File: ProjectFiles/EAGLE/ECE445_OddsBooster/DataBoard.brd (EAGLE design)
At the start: 100 x 80 mm, 51 parts, among them U2 74LV164D-SHIFT_REGISTER, U3 74LV164D-SHIFT_REGISTER, U4 74LV164D-SHIFT_REGISTER, X1 FH12-40S-0.5SH

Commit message: layout minor changes
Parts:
- moved R13 90.6 mm to (29.0, 35.1)
- moved MIC2169 77.0 mm to (20.2, 26.4)
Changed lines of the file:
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@@
 <attribute name="VALUE" x="1.397" y="-7.5565" size="1.27" layer="27"/>
 </element>
-<element name="MIC2169" library="pinhead" library_urn="urn:adsk.eagle:library:325" package="2X05" package3d_urn="urn:adsk.eagle:package:22470/2" value="" x="6.858" y="-49.403" smashed="yes">
-<attribute name="NAME" x="0.508" y="-46.228" size="1.27" layer="25" ratio="10"/>
-<attribute name="POPULARITY" value="35" x="6.858" y="-30.861" size="1.778" layer="27" display="off"/>
-<attribute name="VALUE" x="0.508" y="-53.848" size="1.27" layer="27"/>
+<element name="MIC2169" library="pinhead" library_urn="urn:adsk.eagle:library:325" package="2X05" package3d_urn="urn:adsk.eagle:package:22470/2" value="" x="20.193" y="26.416" smashed="yes">
+<attribute name="NAME" x="13.843" y="29.591" size="1.27" layer="25" ratio="10"/>
+<attribute name="POPULARITY" value="35" x="20.193" y="44.958" size="1.778" layer="27" display="off"/>
+<attribute name="VALUE" x="13.843" y="21.971" size="1.27" layer="27"/>
 </element>
 <element name="R9" library="rcl" library_urn="urn:adsk.eagle:library:334" package="R0805" package3d_urn="urn:adsk.eagle:package:23553/2" value="4k" x="11.43" y="-67.564" smashed="yes">
@@
 <attribute name="VALUE" x="4.318" y="-57.658" size="1.27" layer="27" ratio="10"/>
 </element>
-<element name="R13" library="rcl" library_urn="urn:adsk.eagle:library:334" package="R0805" package3d_urn="urn:adsk.eagle:package:23553/2" value="1.5k" x="20.574" y="-55.118" smashed="yes">
-<attribute name="NAME" x="19.939" y="-53.848" size="1.27" layer="25"/>
-<attribute name="POPULARITY" value="85" x="2.032" y="-112.522" size="1.778" layer="27" display="off"/>
-<attribute name="SPICEPREFIX" value="R" x="2.032" y="-112.522" size="1.778" layer="27" display="off"/>
-<attribute name="VALUE" x="19.939" y="-57.658" size="1.27" layer="27"/>
+<element name="R13" library="rcl" library_urn="urn:adsk.eagle:library:334" package="R0805" package3d_urn="urn:adsk.eagle:package:23553/2" value="1.5k" x="28.956" y="35.052" smashed="yes">
+<attribute name="NAME" x="28.321" y="36.322" size="1.27" layer="25"/>
+<attribute name="POPULARITY" value="85" x="10.414" y="-22.352" size="1.778" layer="27" display="off"/>
+<attribute name="SPICEPREFIX" value="R" x="10.414" y="-22.352" size="1.778" layer="27" display="off"/>
+<attribute name="VALUE" x="28.321" y="32.512" size="1.27" layer="27"/>
 </element>
 <element name="R14" library="pot" library_urn="urn:adsk.eagle:library:331" package="3223G" package3d_urn="urn:adsk.eagle:package:22722/1" value="1k" x="17.78" y="-29.972" smashed="yes">
@@
 <wire x1="6.985" y1="-24.13" x2="7.173" y2="-17.399" width="0" layer="19" extent="1-1"/>
 <wire x1="15.58" y1="-28.572" x2="6.985" y2="-24.13" width="0" layer="19" extent="1-1"/>
-<wire x1="11.938" y1="-48.133" x2="15.58" y2="-28.572" width="0" layer="19" extent="1-1"/>
-<wire x1="8.189" y1="-61.341" x2="11.938" y2="-48.133" width="0" layer="19" extent="1-1"/>
+<wire x1="25.273" y1="27.686" x2="15.58" y2="-28.572" width="0" layer="19" extent="1-1"/>
+<wire x1="8.189" y1="-61.341" x2="25.273" y2="27.686" width="0" layer="19" extent="1-1"/>
 <wire x1="2.982" y1="-61.341" x2="8.189" y2="-61.341" width="0" layer="19" extent="1-1"/>
 <wire x1="2.982" y1="-67.564" x2="2.982" y2="-61.341" width="0" layer="19" extent="1-1"/>
@@
 <wire x1="2.982" y1="-102.616" x2="8.824" y2="-96.393" width="0" layer="19" extent="1-1"/>
 <wire x1="12.065" y1="-109.347" x2="2.982" y2="-102.616" width="0" layer="19" extent="1-1"/>
-<wire x1="26.858" y1="-55.118" x2="11.938" y2="-48.133" width="0" layer="19" extent="1-1"/>
+<wire x1="26.858" y1="-55.118" x2="25.273" y2="27.686" width="0" layer="19" extent="1-1"/>
 <wire x1="6.162" y1="12.446" x2="10.734" y2="-11.176" width="0" layer="19" extent="1-1"/>
 </signal>
@@
 <contactref element="JP2" pad="1"/>
 <wire x1="1.082" y1="-61.341" x2="1.905" y2="-109.347" width="0" layer="19" extent="1-1"/>
-<wire x1="1.778" y1="-50.673" x2="1.082" y2="-61.341" width="0" layer="19" extent="1-1"/>
+<wire x1="15.113" y1="25.146" x2="1.082" y2="-61.341" width="0" layer="19" extent="1-1"/>
 <wire x1="18.603" y1="-61.341" x2="1.082" y2="-61.341" width="0" layer="19" extent="1-1"/>
 </signal>
@@
 <contactref element="D1" pad="A"/>
 <wire x1="11.684" y1="-55.118" x2="1.082" y2="-67.564" width="0" layer="19" extent="1-1"/>
-<wire x1="4.318" y1="-50.673" x2="11.684" y2="-55.118" width="0" layer="19" extent="1-1"/>
+<wire x1="17.653" y1="25.146" x2="11.684" y2="-55.118" width="0" layer="19" extent="1-1"/>
 </signal>
 <signal name="N$6">
 <contactref element="R10" pad="1"/>
 <contactref element="MIC2169" pad="6"/>
-<wire x1="6.858" y1="-48.133" x2="11.496" y2="-61.341" width="0" layer="19" extent="1-1"/>
+<wire x1="20.193" y1="27.686" x2="11.496" y2="-61.341" width="0" layer="19" extent="1-1"/>
 </signal>
 <signal name="N$4">
@@
 <contactref element="R11" pad="1"/>
 <contactref element="MIC2169" pad="5"/>
-<wire x1="6.858" y1="-50.673" x2="16.703" y2="-61.341" width="0" layer="19" extent="1-1"/>
+<wire x1="20.193" y1="25.146" x2="16.703" y2="-61.341" width="0" layer="19" extent="1-1"/>
 </signal>
 <signal name="N$9">
@@
 <contactref element="MIC2169" pad="7"/>
 <wire x1="24.958" y1="-55.118" x2="21.783" y2="-61.341" width="0" layer="19" extent="1-1"/>
-<wire x1="9.398" y1="-50.673" x2="24.958" y2="-55.118" width="0" layer="19" extent="1-1"/>
+<wire x1="22.733" y1="25.146" x2="24.958" y2="-55.118" width="0" layer="19" extent="1-1"/>
 </signal>
 <signal name="N$11">
@@
 <contactref element="MIC2169" pad="2"/>
 <wire x1="1.524" y1="-55.118" x2="5.781" y2="-67.564" width="0" layer="19" extent="1-1"/>
-<wire x1="1.778" y1="-48.133" x2="1.524" y2="-55.118" width="0" layer="19" extent="1-1"/>
+<wire x1="15.113" y1="27.686" x2="1.524" y2="-55.118" width="0" layer="19" extent="1-1"/>
 </signal>
 <signal name="V_CHARGE">
@@
 <contactref element="MIC2169" pad="9"/>
 <contactref element="R13" pad="2"/>
-<wire x1="11.938" y1="-50.673" x2="14.29" y2="-55.118" width="0" layer="19" extent="1-1"/>
-<wire x1="21.524" y1="-55.118" x2="14.29" y2="-55.118" width="0" layer="19" extent="1-1"/>
+<wire x1="25.273" y1="25.146" x2="14.29" y2="-55.118" width="0" layer="19" extent="1-1"/>
+<wire x1="29.906" y1="35.052" x2="14.29" y2="-55.118" width="0" layer="19" extent="1-1"/>
 </signal>
 <signal name="N$14">
 <contactref element="R13" pad="1"/>
 <contactref element="R14" pad="3"/>
-<wire x1="15.58" y1="-31.372" x2="19.624" y2="-55.118" width="0" layer="19" extent="1-1"/>
+<wire x1="28.006" y1="35.052" x2="15.58" y2="-31.372" width="0" layer="19" extent="1-1"/>
 </signal>
 <signal name="N$16">

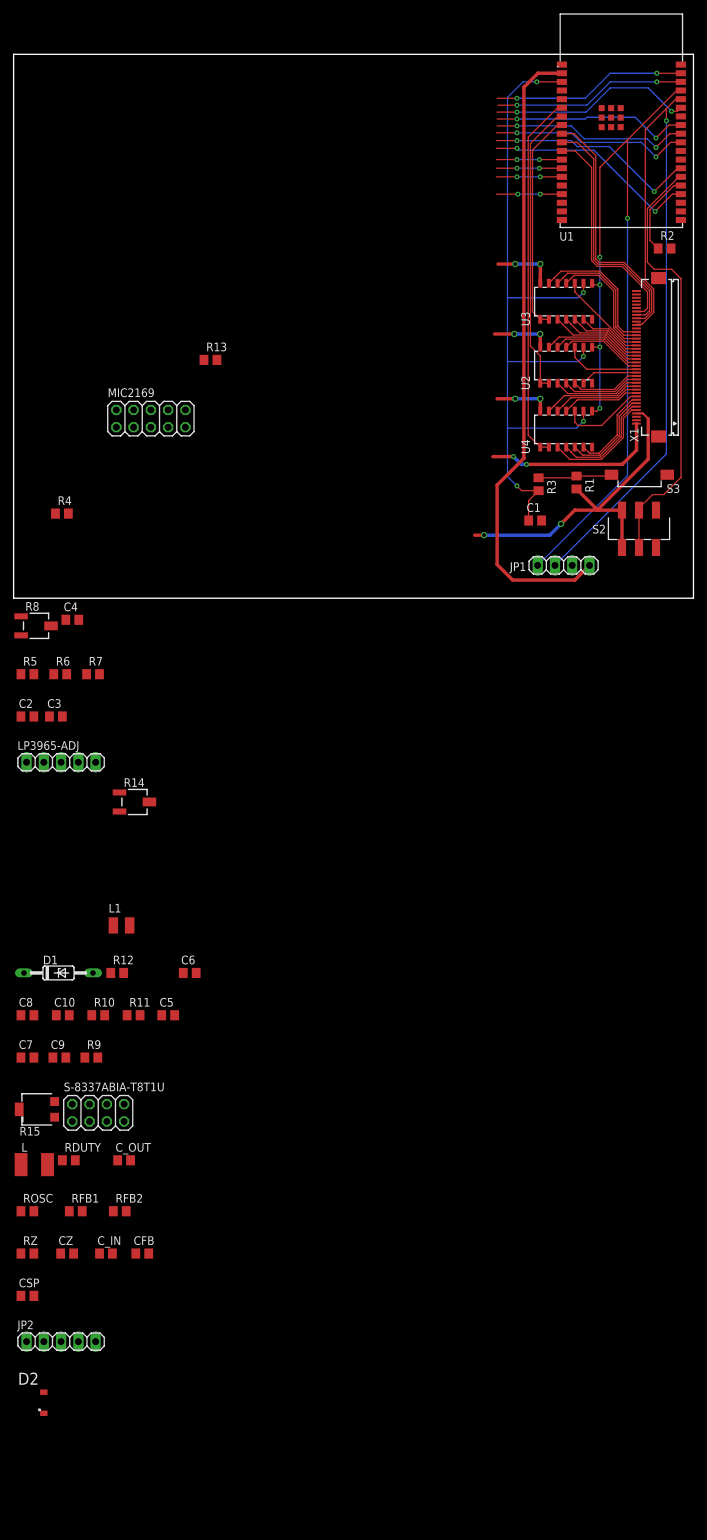
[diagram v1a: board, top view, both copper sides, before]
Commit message: updated data sheets and some layout changes
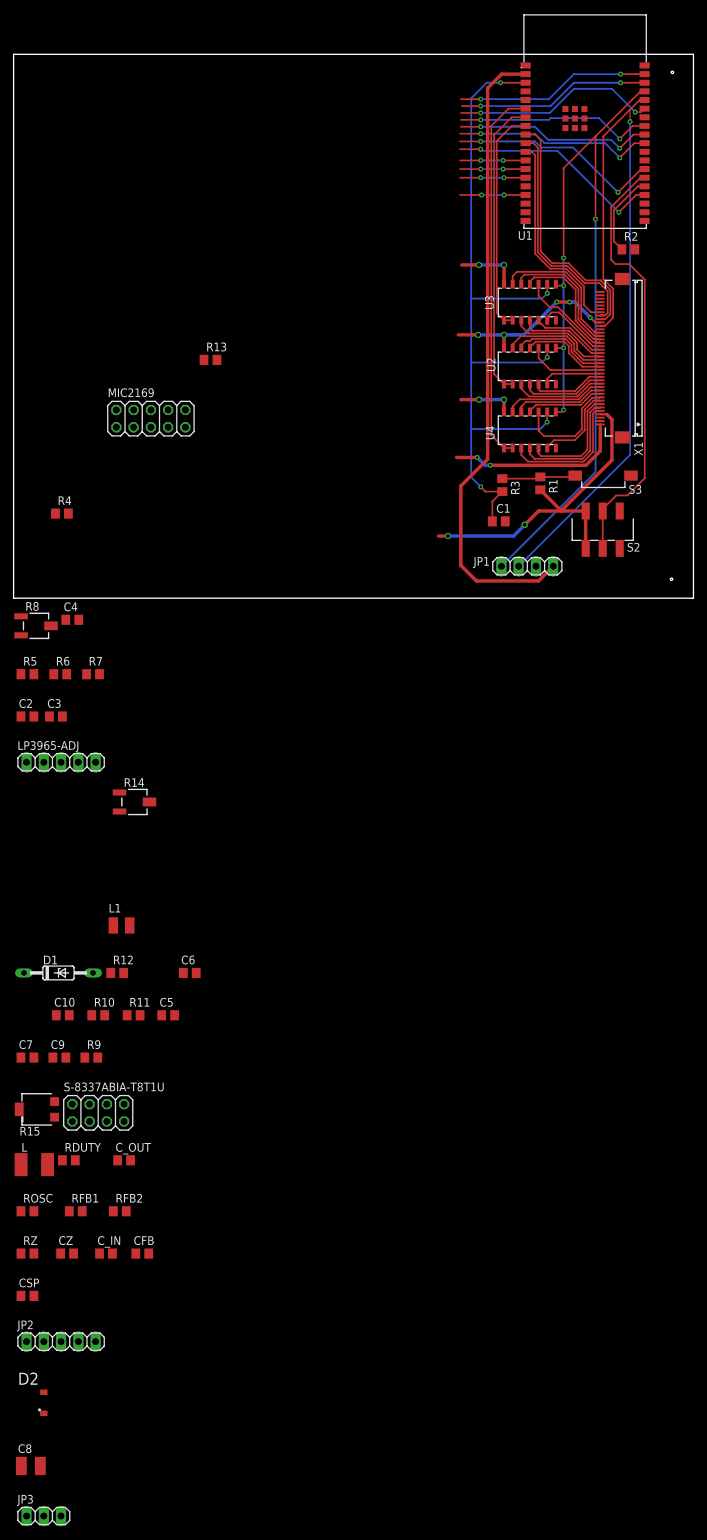
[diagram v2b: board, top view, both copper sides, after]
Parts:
- added JP3: (no value), pinhead:1X03
- C8: device rcl:C0805 -> rcl:C1210
- moved C8 66.3 mm to (2.54, -127.6)
- moved C1 5.34 mm to (71.4, 11.3)
- moved JP1 5.34 mm to (75.6, 4.70)
- moved R1 5.34 mm to (77.5, 16.9)
- moved S2 5.34 mm to (89.2, 12.8)
- moved U2 5.34 mm to (72.1, 31.5)
- moved U3 5.34 mm to (72.1, 40.9)
- moved U4 5.34 mm to (72.1, 22.1)
- moved X1 5.34 mm to (89.5, 35.3)
- moved R2 5.34 mm to (90.4, 51.3)
- moved R3 5.34 mm to (71.9, 16.6)
- moved S3 5.34 mm to (90.8, 18.0)
- moved U1 5.34 mm to (75.3, 78.4)
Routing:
- net VCC: track 77.6 -> 95.0 mm, vias 8 -> 11
- net R4: track 12.7 -> 16.3 mm
- net DE: track 33.4 -> 30.8 mm
- net R0: track 17.0 -> 19.5 mm
- net R1: track 15.7 -> 18.0 mm
- net R2: track 14.4 -> 16.5 mm
- net B3: track 9.39 -> 10.6 mm
- net R_IN: track 54.3 -> 55.5 mm
- net VSYNC: track 35.8 -> 34.6 mm
- net G7: track 14.8 -> 16.0 mm
- net B0: track 13.8 -> 14.9 mm
- net G6: track 13.5 -> 14.5 mm
- net CLK_52: track 124.3 -> 125.1 mm
- net G_IN: track 43.4 -> 44.2 mm
- net B_IN: track 32.5 -> 33.2 mm
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
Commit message: footprints, schematic building, component checks
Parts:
- removed C10: 150u, rcl:C0805
- removed C2: 68u, rcl:C0805
- removed C9, CSP, C_IN: 0.1u, rcl:C0805
- removed CFB: 180p, rcl:C0805
- removed CZ: 0.01u, rcl:C0805
- removed C_OUT: 10u, rcl:C0805
- removed D2: DB2X20700L-DIODE, OddsBooster:DB2X20700L-DIODE
- removed JP2: USB-B Micro, pinhead:1X05
- removed JP3: (no value), pinhead:1X03
- removed L: 10u, rcl:L1812
- removed LP3965-ADJ: (no value), pinhead:1X05
- removed MIC2169: (no value), pinhead:2X05
- removed R11: 560, rcl:R0805
- removed R12, RFB2: 8.2k, rcl:R0805
- removed R13: 1.5k, rcl:R0805
- removed R14: 1k, pot:3223G
- removed R15: 2k, pot:SM-42/43B
- removed RDUTY: 240k, rcl:R0805
- removed RFB1: 82k, rcl:R0805
- removed ROSC: 280k, rcl:R0805
- removed RZ: 200k, rcl:R0805
- removed S-8337ABIA-T8T1U: (no value), pinhead:2X04
- added BSH, DMG1, DMG2: DMG2302UQ-AND-BSH105-NMOS, OddsBooster:DMG2302UQ-AND-BSH105-NMOS
- added C13: 100p, rcl:C0805
- added C14, CSP1, C_IN1: 0.1u, rcl:C0805
- added C16: 100u, rcl:C1210
- added CFB1: 180p, rcl:C0805
- added CZ1: 0.01u, rcl:C0805
- added C_OUT1: 10u, rcl:C0805
- added D4: DB2X20700L-DIODE, OddsBooster:DB2X20700L-DIODE
- added JP4: USB-B Micro, pinhead:1X05
- added JP5: (no value), pinhead:1X03
- added L2: 10u, OddsBooster:SRP0415-BOURNS-100K-10U
- added R16, R19: 10k, rcl:R0805
- added R17, R18: 33k, rcl:R0805
- added R20: 2k, pot:3223G
- added RDUTY1: 240k, rcl:R0805
- added RFB3: 82k, rcl:R0805
- added RFB4: 8.2k, rcl:R0805
- added ROSC1: 280k, rcl:R0805
- added RZ1: 200k, rcl:R0805
- added U5: LP3965-ADJ-LDO, OddsBooster:LP3965-ADJ-LDO
- added U6: MIC2169-BUCK, OddsBooster:MIC2169-BUCK
- added U7: S-8337ABIA-T8T1U-BOOSTCONVERTER, OddsBooster:S-8337ABIA-T8T1U-BOOSTCONVERTER
- added X2: XH-BAT-CONN, OddsBooster:XH-BAT-CONN
- C3: value 33u -> 150p
- C4: value 100p -> 0.1p; device rcl:C0805 -> rcl:C0603
- C5: value 0.1p -> 68u; device rcl:C0805 -> rcl:C1206
- C6: value 150p -> 33u; device rcl:C0805 -> OddsBooster:NEMCO-33U-TANT-CAP
- C7: value 4.7u -> 150u; device rcl:C0805 -> OddsBooster:KEMET-T491-150U-TANT
- C8: value 100u -> 4.7u; device rcl:C1210 -> rcl:C0603
- D1: value Diode -> SL34A-DIODE; device diode:DO35Z10 -> OddsBooster:SL34A-DIODE
- L1: value 3.3u -> SRP0415-BOURNS-100K-10U; device rcl:L2825P -> OddsBooster:SRP0415-BOURNS-100K-10U
- R10: value 2 -> 1k; device rcl:R0805 -> OddsBooster:BOURNS-3316P-2KPOT
- R4: value 10k -> 4k
- R5: value 33k -> 2
- R6: value 33k -> 560
- R7: value 10k -> 8.2k
- R8: value 2k -> 1.5k; device pot:3223G -> rcl:R0805
- R9: value 4k -> BOURNS-3316P-2KPOT; device rcl:R0805 -> OddsBooster:BOURNS-3316P-2KPOT
- X1: value FH12-40S-0.5SH -> FH40-40S-HIROSE-FPC; device con-hirose:FH12-40S-0.5SH -> OddsBooster:FH40-40S-HIROSE-FPC
- moved C4 325.0 mm to (-31.6, -325.6)
- moved D1 287.3 mm to (-32.0, -339.9)
- moved R10 277.3 mm to (-23.7, -336.3)
- moved C7 247.2 mm to (-31.4, -312.5)
- moved R4 219.5 mm to (11.4, -207.0)
- moved R8 197.0 mm to (13.1, -200.8)
- moved R5 196.3 mm to (15.6, -207.0)
- moved C8 196.0 mm to (-31.6, -320.7)
- moved R6 190.9 mm to (28.8, -200.8)
- moved R7 189.7 mm to (7.75, -200.8)
- moved C6 187.2 mm to (-14.1, -238.0)
- moved C3 183.8 mm to (18.4, -200.8)
- moved C5 167.5 mm to (-5.46, -226.4)
- moved L1 157.9 mm to (-6.22, -204.5)
- moved R9 154.3 mm to (1.40, -221.5)
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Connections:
- removed net N$10: MIC2169.5, R11.1
- removed net N$11: C9.1, D1.C, MIC2169.2
- removed net N$12: C5.1, C6.1, MIC2169.7
- removed net N$13: MIC2169.9, R12.1, R13.2
- removed net N$14: R13.1, R14.3
- removed net N$15: D2.P$2, L.2
- removed net N$16: CSP.1, S-8337ABIA-T8T1U.5
- removed net N$17: S-8337ABIA-T8T1U.8
- removed net N$19: CZ.1, RZ.1
- removed net N$20: RZ.2, S-8337ABIA-T8T1U.1
- removed net N$21: CFB.2, RFB1.1, RFB2.2, S-8337ABIA-T8T1U.3
- removed net N$22: ROSC.2, S-8337ABIA-T8T1U.4
- removed net N$23: RDUTY.2, S-8337ABIA-T8T1U.2
- removed net N$24: R15.3, RFB2.1
- removed net N$4: C9.2, L1.1, R10.2
- removed net N$5: MIC2169.8
- removed net N$6: MIC2169.6, R10.1
- removed net N$7: MIC2169.4
- removed net N$8: LP3965-ADJ.1, R7.2
- removed net N$9: C5.2, R9.2
- removed net UART_3V3: JP1.1, U1.2
- removed net UART_GND: JP1.2, U1.38
- new net N$18: C13.2, R16.2, R17.1, R18.1, U5.5
- new net N$25: R19.2, U5.1
- new net N$26: R17.2, R18.2, R20.1
- new net N$27: DMG1.G, U6.9
- new net N$28: DMG2.G, U6.7
- new net N$29: R6.1, U6.3
- new net N$30: C4.2, R4.2
- new net N$31: C3.1, C4.1, U6.4
- new net N$32: C14.1, D1.2
- new net N$33: R7.1, R8.2, U6.5
- new net N$34: R10.P$1, R8.1
- new net N$35: CSP1.1, U7.3
- new net N$36: BSH.G, U7.5
- new net N$37: CZ1.1, RZ1.1
- new net N$38: RZ1.2, U7.1
- new net N$39: CFB1.2, RFB3.1, RFB4.2, U7.2
- new net N$40: ROSC1.2, U7.7
- new net N$41: RDUTY1.2, U7.8
- new net N$42: R9.P$1, RFB4.1
- new net N$43: BSH.D, D4.P$2, L1.P$2
- new net V_IN: C5.1, C_IN1.1, JP5.3, L1.P$1, R19.1, U5.2, U7.4
- net GND: now also BSH.S, C16.2, C5.2, C6.P$1, C7.P$2, CSP1.2, CZ1.2, C_IN1.2, C_OUT1.2, DMG2.S, JP1.2, JP4.5, R10.P$2, R10.P$3, R16.1, R9.P$2, R9.P$3, RDUTY1.1, ROSC1.1, U1.38, U5.3, U6.6, U7.6, X2.P$2; no longer C10.2, C2.2, C6.2, C7.2, CSP.2, CZ.2, C_IN.2, C_OUT.2, JP2.5, LP3965-ADJ.3, MIC2169.10, R14.1, R15.2, R7.1, R9.1, RDUTY.1, ROSC.1, S-8337ABIA-T8T1U.6
- net N$1: now also C14.2, DMG1.S, DMG2.D, L2.P$1, R5.2; no longer C7.1, D1.A, MIC2169.3
- net N$2: now also C8.1, D1.1, U6.10, U6.2; no longer R5.2, R6.2, R8.1
- net N$3: now also U6.8; no longer C4.2, LP3965-ADJ.5, R4.2, R6.1
- net VCC: now also C13.1, C6.P$2, JP1.1, R20.2, U1.2, U5.4; no longer C3.1, C4.1, LP3965-ADJ.4, R8.2
- net VDD: now also CFB1.1, C_OUT1.1, D4.P$1, RFB3.2; no longer CFB.1, C_OUT.1, D2.P$1, RFB1.2
- net V_BAT: now also JP5.2, X2.P$1; no longer C2.1, C_IN.1, L.1, LP3965-ADJ.2, S-8337ABIA-T8T1U.7
- net V_CHARGE: now also C7.P$1, JP5.1, L2.P$2, R7.2; no longer C10.1, L1.2, R12.2
- net V_USB: now also C16.1, DMG1.D, JP4.1, R6.2, U6.1; no longer C8.1, JP2.1, MIC2169.1, R11.2
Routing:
- net UART_3V3: track 93.7 -> 0.00 mm
- net VCC: track 95.0 -> 184.6 mm, vias 11 -> 8
- net G6: track 14.5 -> 73.9 mm, vias 0 -> 2
- net G4: track 11.3 -> 70.0 mm, vias 0 -> 2
- net IO0: track 63.7 -> 5.50 mm
- net G2: track 10.8 -> 64.4 mm, vias 0 -> 2
- net G0: track 13.6 -> 55.1 mm, vias 0 -> 2
- net B0: track 14.9 -> 49.4 mm, vias 0 -> 2
- net B2: track 10.9 -> 42.8 mm, vias 0 -> 2
- net CLK_6.5: track 111.9 -> 80.6 mm, vias 1 -> 2
- net R6: track 13.4 -> 36.3 mm, vias 0 -> 2
- net RESET: track 113.9 -> 134.5 mm
- net B4: track 13.7 -> 34.1 mm, vias 0 -> 2
- net R4: track 16.3 -> 31.5 mm, vias 0 -> 2
- net B6: track 19.2 -> 32.3 mm, vias 0 -> 2
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- added copper zone on layer 1, net GND
- added copper zone on layer 16, net GND

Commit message: eagle updates
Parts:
- added AE1: W3102-ANTENNA, OddsBooster_3_8_6PM:W3102-ANTENNA
- added C10, C15, C21: 15pF, rcl:C0805K
- added C11, C17, C18, C19: 68pF, rcl:C0805K
- added C12: 0.22uF, rcl:C0402
- added C2: 4.7uF, OddsBooster_3_8_6PM:865080640004-ELECTROLYTIC-CAP
- added C20: 8.2pF, rcl:C0402
- added C22, C9: 0.1uF, rcl:C0805
- added L3, L4: 0.1uF, OddsBooster_3_8_6PM:SRP0415-BOURNS-100K-10U
- added R11: 10k, rcl:R0805
- added R12: 820, rcl:R0805
- added R13: 2.7k, rcl:R0805
- added U8: MFRC500, OddsBooster_3_8_6PM:MFRC500
- added X3: CFPX-180-XTAL-OSCILLATOR, OddsBooster_3_8_6PM:CFPX-180-XTAL-OSCILLATOR
- moved X2 378.5 mm to (3.30, 32.1), turned to 270 degrees
- moved R10 353.0 mm to (53.7, 8.13), turned to 270 degrees
- moved D1 348.4 mm to (17.1, 5.08)
- moved C4 336.4 mm to (8.38, 8.38)
- moved C7 329.5 mm to (39.5, 9.27), turned to 180 degrees
- moved C8 328.2 mm to (14.5, 4.32), turned to 270 degrees
- moved L2 320.5 mm to (39.5, 2.03), turned to 90 degrees
- moved DMG2 319.5 mm to (32.1, 2.09), turned to 180 degrees
- moved BSH 304.9 mm to (27.7, 21.3), turned to 90 degrees
- moved DMG1 303.5 mm to (28.6, 3.11), turned to 270 degrees
- moved C6 285.0 mm to (17.9, 45.2), turned to 270 degrees
- moved C5 273.4 mm to (55.8, 40.0), turned to 90 degrees
- moved U6 272.4 mm to (9.77, 14.2), turned to 270 degrees
- moved R9 255.3 mm to (42.5, 30.5), turned to 90 degrees
- moved JP5 242.8 mm to (60.6, 32.3), turned to 90 degrees
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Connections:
- removed net N$32: C14.1, D1.2
- new net 0: C10.1, C11.2, C12.2, C15.1, C17.1, C18.2, C19.1, C2.2-, C22.2, C9.2, R11.2, U8.12, U8.24, U8.28, U8.3, U8.8, U8.9
- new net N$10: C21.1, R13.1
- new net N$11: L3.P$2, U8.5
- new net N$12: L4.P$2, U8.7
- new net N$13: AE1.1, C11.1, C18.1, C20.2, C21.2, L3.P$1
- new net N$14: AE1.2, C17.2, C19.2, C20.1, L4.P$1
- new net N$4: C14.1, D1.2, U6.10
- new net N$5: C10.2, U8.1, X3.1
- new net N$6: C15.2, U8.32, X3.3
- new net N$7: R11.1, U8.31
- new net N$8: C9.1, R12.1, U8.30
- new net N$9: R12.2, R13.2, U8.29
- net ALE: now also U8.21
- net D0: now also U8.13
- net D1: now also U8.14
- net D2: now also U8.15
- net D3: now also U8.16
- net D4: now also U8.17
- net D5: now also U8.18
- net D6: now also U8.19
- net D7: now also U8.20
- net GND: now also U1.40, U1.41, U1.42, U1.43, U1.44, U1.45, U1.46, U1.47
- net IRQ: now also U8.2
- net N$2: no longer U6.10
- net NRD: now also U8.11
- net NWR: now also U8.10
- net VCC: now also C12.1, C2.1+, C22.1, U8.22, U8.23, U8.25, U8.26, U8.6
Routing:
- net V_IN: track 0.00 -> 80.3 mm, vias 0 -> 2
- net VCC: track 184.6 -> 261.2 mm
- net IO0: track 5.50 -> 68.8 mm
- net V_BAT: track 0.00 -> 57.4 mm
- net N$33: track 0.00 -> 56.6 mm, vias 0 -> 2
- net N$25: track 0.00 -> 54.8 mm, vias 0 -> 2
- net V_CHARGE: track 0.00 -> 53.1 mm, vias 0 -> 1
- net VDD: track 38.6 -> 87.8 mm
- net V_USB: track 0.00 -> 45.5 mm
- net N$39: track 0.00 -> 38.1 mm, vias 0 -> 2
- net N$28: track 0.00 -> 31.0 mm, vias 0 -> 2
- net N$4: track 0.00 -> 30.1 mm, vias 0 -> 2
- net N$27: track 0.00 -> 29.2 mm, vias 0 -> 2
- net N$1: track 0.00 -> 28.3 mm
- net N$2: track 0.00 -> 19.1 mm
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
